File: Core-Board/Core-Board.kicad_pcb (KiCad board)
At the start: 2 copper layers, 127 x 101.6 mm, 27 parts, among them J1 POWER, J10 PCIE, J2 PCIE, J3 XT60-M, J4 PCIE, J5 PCIE, J6 ESP32-DEVKITC-32D, J7 Conn_01x19_Male, J8 PCIE, J9 Conn_01x19_Male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

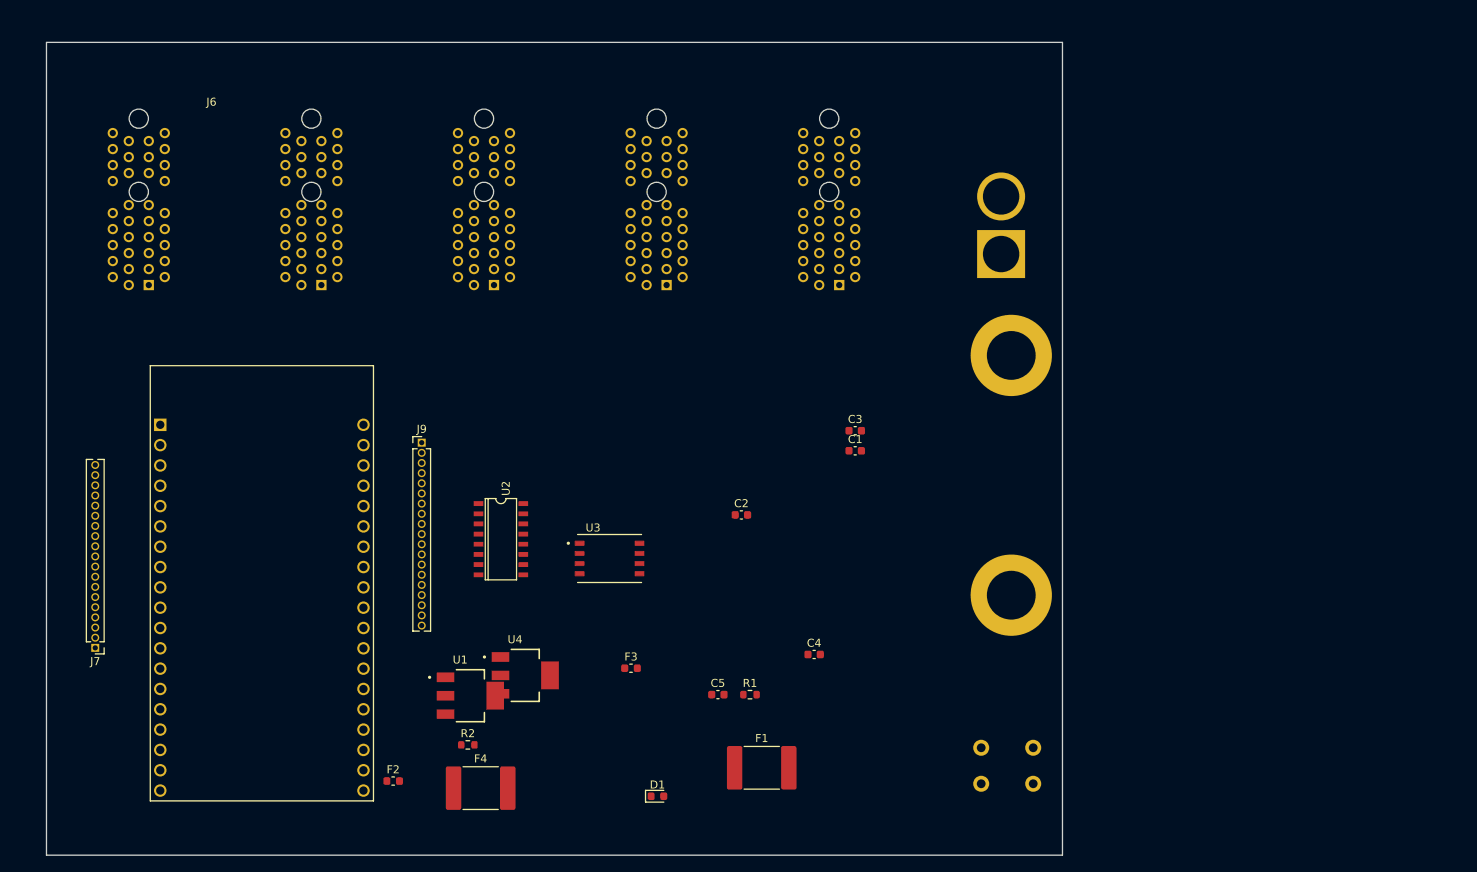
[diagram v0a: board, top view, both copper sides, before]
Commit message: wired pcie together in core board.
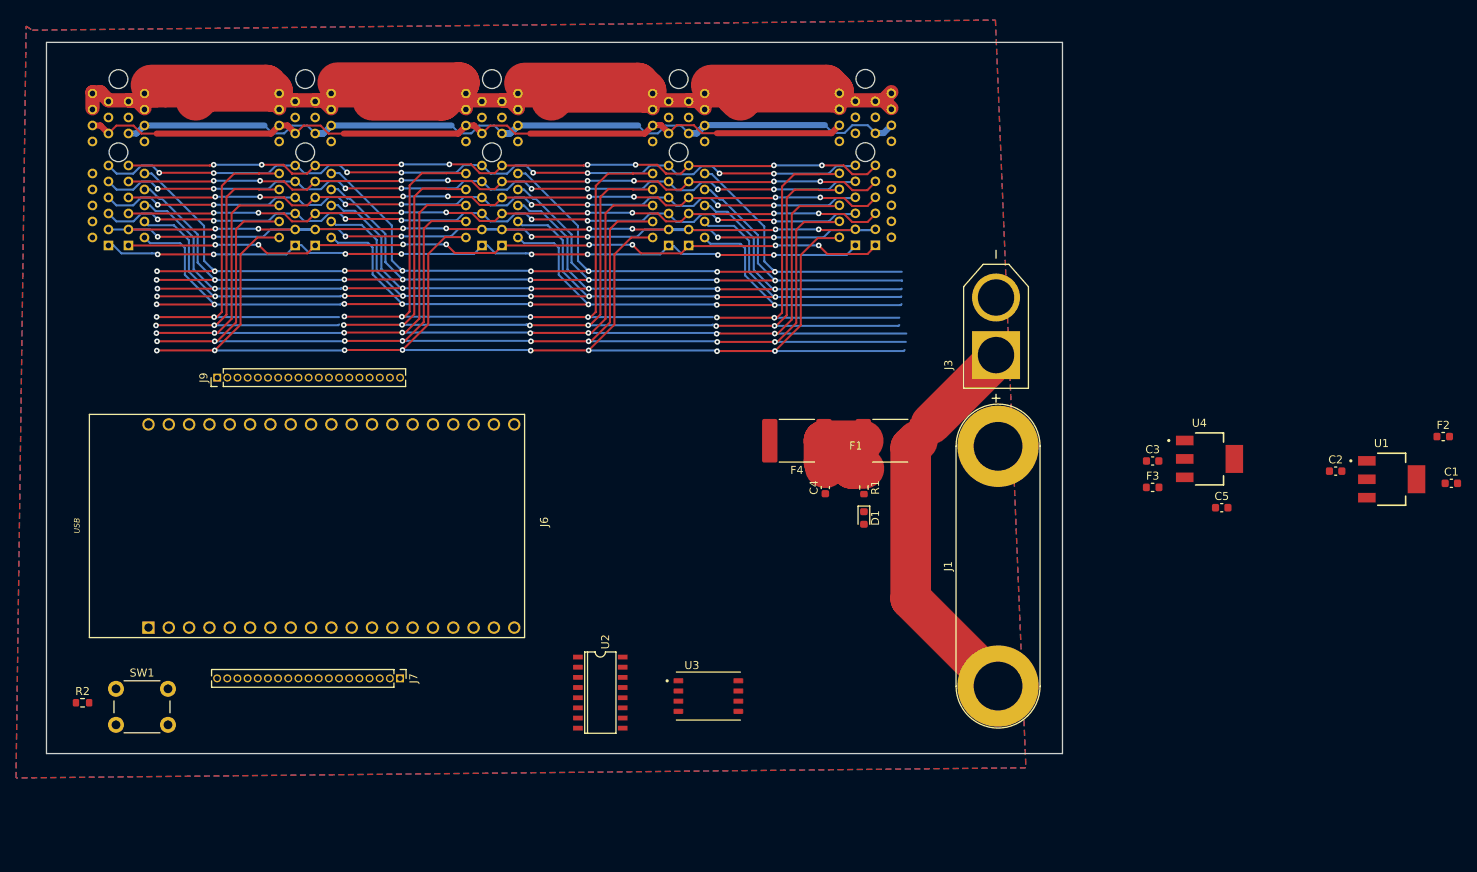
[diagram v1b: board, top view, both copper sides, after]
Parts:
- J1, J3, SW1: moved to F.Cu
- J10, J2, J4, J5, J8: footprint PCIE_throughhole:AMPHENOL_10018783-11200TLF -> 10018784-10210TLF:AMPHENOL_10018784-10210TLF
- moved F2 138.1 mm to (288.9, 112.8)
- moved U1 118.3 mm to (282.4, 118.1)
- moved SW1 114.9 mm to (123.0, 144.3), turned to 0 degrees
- moved U4 89.7 mm to (259.7, 115.6)
- moved C1 74.6 mm to (289.9, 118.6)
- moved C2 74.5 mm to (275.4, 117.1)
- moved F3 69.0 mm to (252.6, 119.1)
- moved C5 67.2 mm to (261.2, 121.7)
- moved F4 58.7 mm to (208.1, 113.3), turned to 180 degrees
- moved R2 48.4 mm to (118.8, 146.1)
- moved F1 43.9 mm to (219.8, 113.3), turned to 180 degrees
- moved D1 43.3 mm to (216.5, 122.9), turned to -90 degrees
- moved J7 38.3 mm to (158.5, 143.0), turned to -90 degrees
- moved C3 37.4 mm to (252.6, 115.8)
- moved R1 29.6 mm to (216.5, 119.1), turned to -90 degrees
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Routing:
- net GND: track 0.00 -> 354.5 mm, vias 0 -> 24
- net 12V: track 0.00 -> 250.4 mm
- net TC2: track 0.00 -> 190.9 mm, vias 0 -> 8
- net HX5: track 0.00 -> 187.0 mm, vias 0 -> 8
- net HX3: track 0.00 -> 184.8 mm, vias 0 -> 8
- net HX1: track 0.00 -> 178.8 mm, vias 0 -> 8
- net SD, TC MISO: track 0.00 -> 170.3 mm, vias 0 -> 8
- net HX CLK: track 0.00 -> 157.8 mm, vias 0 -> 8
- net HX7: track 0.00 -> 154.9 mm, vias 0 -> 8
- net TC CLK: track 0.00 -> 152.2 mm, vias 0 -> 8
- net MOS SCL: track 0.00 -> 149.4 mm, vias 0 -> 8
- net 5V: track 0.00 -> 109.5 mm
- net 3.3V: track 0.00 -> 100.2 mm
- net TC3: track 0.00 -> 99.9 mm, vias 0 -> 8
- net TC1: track 0.00 -> 99.7 mm, vias 0 -> 8
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- added copper zone on B.Cu, net GND
- added copper zone on F.Cu, net GND
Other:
- board size 127 x 101.6 mm -> 127 x 88.9 mm
- board text added: "A1"
- board text added: "B1"
- board text added: "USB"

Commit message: Finish tracing core board. Need to do cleanup and silkscreen.
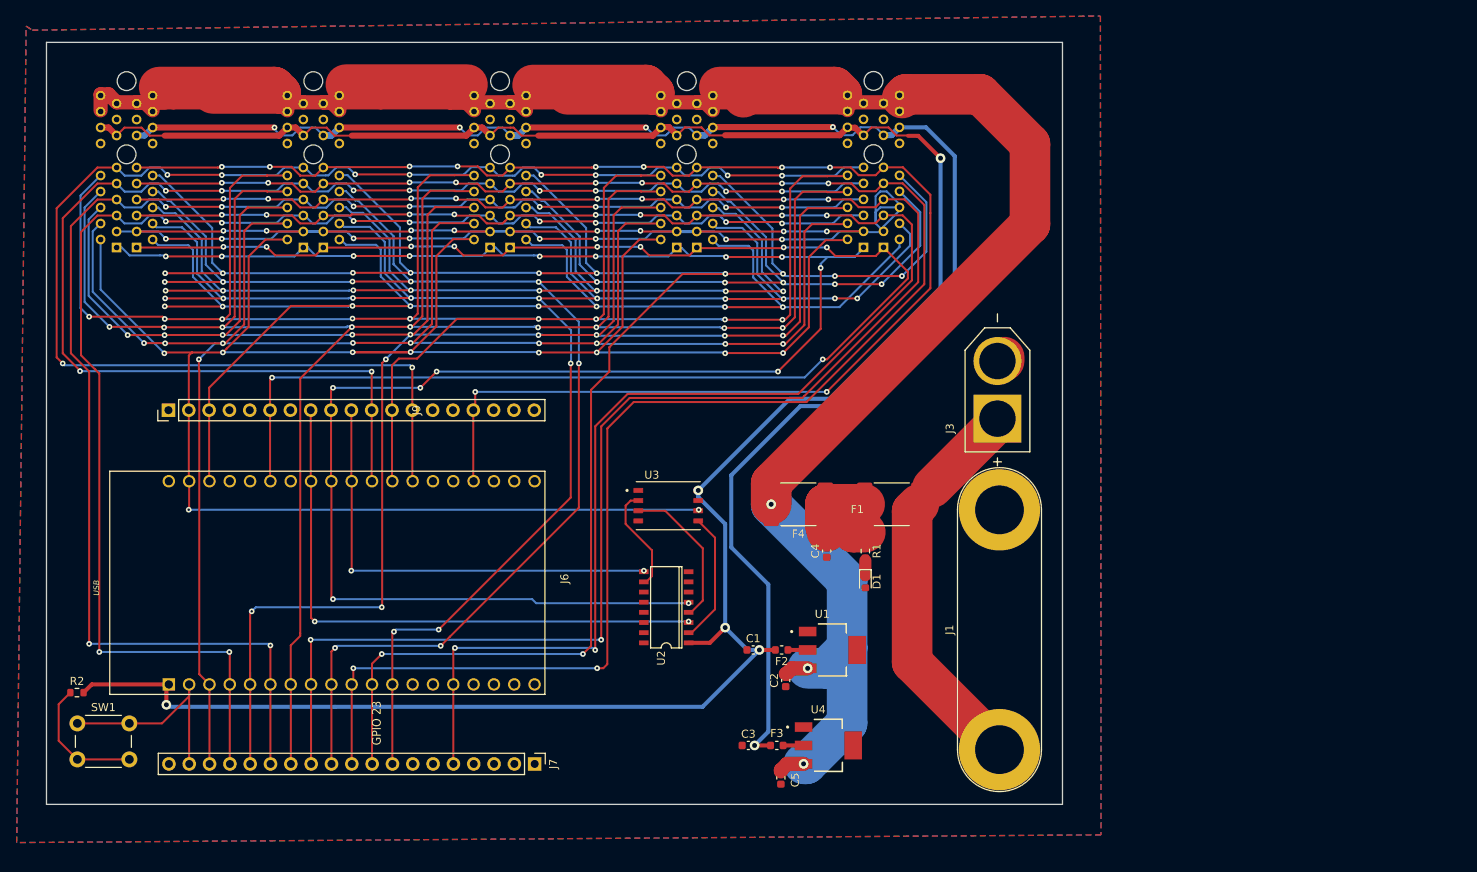
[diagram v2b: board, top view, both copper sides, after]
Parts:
- J7, J9: footprint Connector_PinHeader_1.27mm:PinHeader_1x19_P1.27mm_Vertical -> Connector_PinHeader_2.54mm:PinHeader_1x19_P2.54mm_Vertical
- moved C1 89.7 mm to (202.6, 139.4)
- moved F2 86.9 mm to (206.2, 139.4), turned to 180 degrees
- moved C2 73.6 mm to (206.7, 143.3), turned to 90 degrees
- moved U1 73.1 mm to (212.5, 139.4)
- moved C5 64.6 mm to (206.1, 155.4), turned to 90 degrees
- moved C3 61.8 mm to (202.0, 151.4)
- moved U4 59.6 mm to (212.0, 151.4)
- moved F3 57.0 mm to (205.6, 151.4), turned to 180 degrees
- moved U3 24.3 mm to (192.0, 121.4)
- moved J7 19.9 mm to (175.3, 153.7)
- moved U2 13.5 mm to (191.8, 134.1), turned to 90 degrees
- moved C4 7.95 mm to (211.8, 127.1)
- moved D1 7.95 mm to (216.7, 130.9)
- moved F1 7.95 mm to (220.0, 121.2)
- moved F4 7.95 mm to (208.3, 121.2)
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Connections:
- J6 pad 19: 5V -> unconnected-(J6-Pad19)
- U2 pad 1: +3.3V -> 3.3V
- U3 pad 8: +3.3V -> 3.3V
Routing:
- net 3.3V: track 100.2 -> 294.1 mm, vias 0 -> 5
- net SD, TC CLK: track 97.2 -> 242.3 mm, vias 8 -> 15
- net HX6: track 96.9 -> 236.4 mm, vias 8 -> 10
- net HX8: track 97.0 -> 233.9 mm, vias 8 -> 10
- net TC MISO: track 96.9 -> 216.1 mm, vias 8 -> 10
- net 12V: track 250.4 -> 363.1 mm, vias 0 -> 3
- net HX CLK: track 157.8 -> 269.6 mm, vias 8 -> 12
- net MOS SDA: track 96.9 -> 199.8 mm, vias 8 -> 10
- net 5V: track 109.5 -> 211.1 mm, vias 0 -> 5
- net HX4: track 99.7 -> 197.5 mm, vias 8 -> 10
- net HX7: track 154.9 -> 249.1 mm, vias 8 -> 13
- net SD, TC MISO: track 170.3 -> 262.8 mm, vias 8 -> 10
- net TC4: track 97.9 -> 190.3 mm, vias 8 -> 10
- net HX2: track 99.6 -> 188.9 mm, vias 8 -> 10
- net TC3: track 99.9 -> 187.4 mm, vias 8 -> 10
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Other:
- board size 127 x 88.9 mm -> 127 x 95.2 mm
- board text added: "GPIO 23"

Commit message: Finished core board.
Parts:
- added G***: LOGO, star:star_8x7, F.Cu at (191.2, 101.1)
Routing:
- net HX7: track 249.1 -> 241.6 mm, vias 13 -> 11
- net TC CLK: track 230.6 -> 223.3 mm, vias 13 -> 11
- net MOS SCL: track 186.0 -> 178.8 mm, vias 8 -> 6
- net HX CLK: track 269.6 -> 262.4 mm, vias 12 -> 10
- net HX3: track 264.0 -> 262.4 mm, vias 12 -> 10
- net GND: track 351.6 -> 350.6 mm
- net TC4: track 190.3 -> 189.5 mm
- net TC MISO: track 216.1 -> 215.4 mm
- net 3.3V: track 294.1 -> 293.4 mm
- net SD, TC MISO: track 262.8 -> 262.3 mm, vias 10 -> 9
- net HX5: track 256.2 -> 256.1 mm, vias 9 -> 7
- net HX1: vias 10 -> 8
- net TC2: vias 9 -> 7
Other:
- board text added: "+"
- board text added: "-"
- board text added: "3V3"
- board text added: "Banana plug"
- board text added: "EN"
- board text added: "ESP32-DEVKITC-V4"
- board text added: "GND"
- board text added: "Ground DAQ 2 LE2 Hotfire 2023"
- board text added: "HX CLK"
- board text added: "HX1 DT"
- board text added: "HX2 DT"
- board text added: "HX3 DT"
- board text added: "HX4 DT"
- board text added: "HX5 DT"
- board text added: "HX6 DT"
- board text added: "HX7 DT"
- board text added: "HX8 DT"
- board text added: "I2C SCL"
- board text added: "I2C SDA"
- board text added: "PERIPHERAL 1"
- board text added: "PERIPHERAL 2"
- board text added: "PERIPHERAL 3"
- board text added: "PERIPHERAL 4"
- board text added: "PERIPHERAL 5"
- board text added: "SD CLK"
- board text added: "SD CS"
- board text added: "SD MISO"
- board text added: "SD MOSI"
- board text added: "TC CLK"
- board text added: "TC MISO"
- board text added: "TC1 CS"
- board text added: "TC2 CS"
- board text added: "TC3 CS"
- board text added: "TC4 CS"
- board text added: "This side up"
- board text added: "Wrong side"
- board text added: "XT-60"
- board text removed: "GPIO 23"
- board text removed: "USB"

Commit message: final vers
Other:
- board text added: "Designed by: Khai Sam"
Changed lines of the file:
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@@
     (effects (font (size 1.1 1) (thickness 0.15)))
+  )
+  (gr_text "Designed by:\nKhai Sam " (at 191.008 151.892) (layer "F.SilkS")
+    (effects (font (size 1 0.7) (thickness 0.15)))
   )
   (gr_text "HX1 DT" (at 134.6962 148.7932 90) (layer "F.SilkS")
